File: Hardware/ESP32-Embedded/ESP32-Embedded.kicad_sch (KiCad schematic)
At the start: 20 parts, among them J1 10103592-0001LF, Q1 S8050, Q2 S8050, U1 ESP32-WROOM-32E, U2 AMS1117-3.3, U3 CH340G

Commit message: sch casi terminado ordene y agregue pocas cosas
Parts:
- added R6: 10K, EESTN5:R_1206, symbol Device:R
- added SW1, SW2: SW_Push, symbol EESTN5:SW_Push
- C6: value C_Small -> 100nF
- J1: value 10103592-0001LF -> Micro USB
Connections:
- net +3V3: now also R6.2
- net EN: now also SW1.2
- net GND: now also SW1.1, SW2.1
- net IO0: now also R6.1, SW2.2
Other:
- note added: "Alimentacion"
- note added: "Conversor UART/Serial"
- note added: "ESP32 WROOM 32"
- note added: "Pulsadores EN y BOOT , y Led test Blink"
- moved on the sheet: C1, C2, C3, C4, C5, C6, D1, J1, LED1, LED2, Q1, Q2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

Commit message: sch terminado
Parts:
- added C7, C8: 22pF, symbol Device:C_Small
- added C9: 100nF, symbol Device:C_Small
- added Y1: 12Mhz, symbol Device:Crystal
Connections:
- net +3V3: now also C9.2
- net GND: now also C7.2, C8.2, C9.1
- net at U3.7 (XI): now also C7.1, Y1.1
- net at U3.8 (XO): now also C8.1, Y1.2
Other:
- moved on the sheet: C5

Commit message: agregue foots ,inicie pcb ordene componentes
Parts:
- C1, C3: footprint EESTN5:C_0805 -> Capacitor_THT:CP_Radial_D4.0mm_P1.50mm
- C5, C9: footprint (none) -> EESTN5:C_0805
- C6: renamed from C7; footprint (none) -> EESTN5:C_1206
- C7: renamed from C8; footprint (none) -> EESTN5:C_1206
- C8: renamed from C6; footprint (none) -> EESTN5:C_0805
- D1: footprint (none) -> Diode_SMD:D_SMF
- J1: footprint AMPHENOL_10103592-0001LF -> MICROUSB FOOT:AMPHENOL_10103592-0001LF
- Q1, Q2: footprint Package_TO_SOT_THT:TO-92_Inline -> SS8050:SOT-23_BEC
- R2, R3: footprint (none) -> EESTN5:R_1206
- SW1, SW2: footprint (none) -> Button_Switch_SMD:SW_SPST_B3U-1000P-B
- U1: footprint footprints:ESP32-WROOM-32E -> ESP32-WROOM-32D:MODULE_ESP32-WROOM-32D
- U2: footprint footprints:SOT-223-3_TabPin2 -> Package_TO_SOT_SMD:SOT-223-3_TabPin2
- Y1: footprint (none) -> Crystal:Crystal_SMD_3215-2Pin_3.2x1.5mm
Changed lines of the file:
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@@
   (symbol (lib_id "Device:C_Small") (at 202.565 48.514 0) (unit 1)
     (in_bom yes) (on_board yes) (dnp no) (fields_autoplaced)
-    (property "Reference" "C6" (at 204.8891 47.8766 0)
+    (property "Reference" "C8" (at 204.8891 47.8766 0)
       (effects (font (size 1.27 1.27)) (justify left))
     )
@@
       (effects (font (size 1.27 1.27)) (justify left))
     )
-    (property "Footprint" "" (at 202.565 48.514 0)
+    (property "Footprint" "EESTN5:C_0805" (at 202.565 48.514 0)
       (effects (font (size 1.27 1.27)) hide)
     )
@@
       (project "ESP32-Embedded"
         (path "/44ee4593-0772-40e5-aa53-983b9011845a"
-          (reference "C6") (unit 1)
+          (reference "C8") (unit 1)
         )
       )
@@
       (effects (font (size 1.27 1.27)) (justify left))
     )
-    (property "Footprint" "EESTN5:C_0805" (at 61.6712 120.523 0)
+    (property "Footprint" "Capacitor_THT:CP_Radial_D4.0mm_P1.50mm" (at 61.6712 120.523 0)
       (effects (font (size 1.27 1.27)) hide)
     )
@@
   (symbol (lib_id "Device:C_Small") (at 15.24 63.627 0) (unit 1)
     (in_bom yes) (on_board yes) (dnp no)
-    (property "Reference" "C7" (at 18.796 63.373 0)
+    (property "Reference" "C6" (at 18.796 63.373 0)
       (effects (font (size 1.27 1.27)))
     )
@@
       (effects (font (size 1.27 1.27)))
     )
-    (property "Footprint" "" (at 15.24 63.627 0)
+    (property "Footprint" "EESTN5:C_1206" (at 15.24 63.627 0)
       (effects (font (size 1.27 1.27)) hide)
     )
@@
       (project "ESP32-Embedded"
         (path "/44ee4593-0772-40e5-aa53-983b9011845a"
-          (reference "C7") (unit 1)
+          (reference "C6") (unit 1)
         )
       )
@@
       (effects (font (size 1.27 1.27)))
     )
-    (property "Footprint" "" (at 21.082 57.658 0)
+    (property "Footprint" "Crystal:Crystal_SMD_3215-2Pin_3.2x1.5mm" (at 21.082 57.658 0)
       (effects (font (size 1.27 1.27)) hide)
     )
@@
       (effects (font (size 1.27 1.27)))
     )
-    (property "Footprint" "AMPHENOL_10103592-0001LF" (at 24.257 117.729 0)
+    (property "Footprint" "MICROUSB FOOT:AMPHENOL_10103592-0001LF" (at 24.257 117.729 0)
       (effects (font (size 1.27 1.27)) (justify bottom) hide)
     )
@@
       (effects (font (size 1.27 1.27)))
     )
-    (property "Footprint" "" (at 127.381 44.577 0)
+    (property "Footprint" "EESTN5:C_0805" (at 127.381 44.577 0)
       (effects (font (size 1.27 1.27)) hide)
     )
@@
       (effects (font (size 1.27 1.27)))
     )
-    (property "Footprint" "footprints:SOT-223-3_TabPin2" (at 78.486 106.553 0)
+    (property "Footprint" "Package_TO_SOT_SMD:SOT-223-3_TabPin2" (at 78.486 106.553 0)
       (effects (font (size 1.27 1.27)) hide)
     )
@@
       (effects (font (size 1.27 1.27)) (justify left))
     )
-    (property "Footprint" "Package_TO_SOT_THT:TO-92_Inline" (at 93.345 43.18 0)
+    (property "Footprint" "SS8050:SOT-23_BEC" (at 93.345 43.18 0)
       (effects (font (size 1.27 1.27) italic) (justify left) hide)
     )
@@
       (effects (font (size 1.27 1.27)))
     )
-    (property "Footprint" "" (at 77.089 41.275 0)
+    (property "Footprint" "EESTN5:R_1206" (at 77.089 41.275 0)
       (effects (font (size 1.27 1.27)) hide)
     )
@@
       (effects (font (size 1.27 1.27)))
     )
-    (property "Footprint" "" (at 42.545 125.349 0)
+    (property "Footprint" "Diode_SMD:D_SMF" (at 42.545 125.349 0)
       (effects (font (size 1.27 1.27)) hide)
     )
@@
   (symbol (lib_id "Device:C_Small") (at 25.781 63.881 0) (unit 1)
     (in_bom yes) (on_board yes) (dnp no)
-    (property "Reference" "C8" (at 29.083 65.405 0)
+    (property "Reference" "C7" (at 29.083 65.405 0)
       (effects (font (size 1.27 1.27)))
     )
@@
       (effects (font (size 1.27 1.27)))
     )
-    (property "Footprint" "" (at 25.781 63.881 0)
+    (property "Footprint" "EESTN5:C_1206" (at 25.781 63.881 0)
       (effects (font (size 1.27 1.27)) hide)
     )
@@
       (project "ESP32-Embedded"
         (path "/44ee4593-0772-40e5-aa53-983b9011845a"
-          (reference "C8") (unit 1)
+          (reference "C7") (unit 1)
         )
       )
@@
       (effects (font (size 1.27 1.27)) (justify left))
     )
-    (property "Footprint" "Package_TO_SOT_THT:TO-92_Inline" (at 93.345 60.198 0)
+    (property "Footprint" "SS8050:SOT-23_BEC" (at 93.345 60.198 0)
       (effects (font (size 1.27 1.27) italic) (justify left) hide)
     )
@@
       (effects (font (size 1.27 1.27)))
     )
-    (property "Footprint" "" (at 77.089 58.293 0)
+    (property "Footprint" "EESTN5:R_1206" (at 77.089 58.293 0)
       (effects (font (size 1.27 1.27)) hide)
     )
@@
       (effects (font (size 1.27 1.27)) hide)
     )
-    (property "Footprint" "" (at 235.585 54.737 0)
-      (effects (font (size 1.27 1.27)))
+    (property "Footprint" "Button_Switch_SMD:SW_SPST_B3U-1000P-B" (at 235.585 54.737 0)
+      (effects (font (size 1.27 1.27)) hide)
     )
     (property "Datasheet" "" (at 235.585 54.737 0)
@@
       (effects (font (size 1.27 1.27)) hide)
     )
-    (property "Footprint" "" (at 216.281 54.61 0)
-      (effects (font (size 1.27 1.27)))
+    (property "Footprint" "Button_Switch_SMD:SW_SPST_B3U-1000P-B" (at 216.281 54.61 0)
+      (effects (font (size 1.27 1.27)) hide)
     )
     (property "Datasheet" "" (at 216.281 54.61 0)
@@
   (symbol (lib_id "Device:C_Small") (at 51.435 64.008 270) (unit 1)
     (in_bom yes) (on_board yes) (dnp no)
-    (property "Reference" "C5" (at 49.911 67.818 90)
+    (property "Reference" "C5" (at 48.006 67.818 90)
       (effects (font (size 1.27 1.27)))
     )
@@
       (effects (font (size 1.27 1.27)))
     )
-    (property "Footprint" "" (at 51.435 64.008 0)
+    (property "Footprint" "EESTN5:C_0805" (at 51.435 64.008 0)
       (effects (font (size 1.27 1.27)) hide)
     )
@@
       (effects (font (size 1.27 1.27)) (justify left))
     )
-    (property "Footprint" "EESTN5:C_0805" (at 89.3572 120.523 0)
+    (property "Footprint" "Capacitor_THT:CP_Radial_D4.0mm_P1.50mm" (at 89.3572 120.523 0)
       (effects (font (size 1.27 1.27)) hide)
     )
@@
       (effects (font (size 1.27 1.27)) (justify left))
     )
-    (property "Footprint" "footprints:ESP32-WROOM-32E" (at 152.019 67.183 0)
+    (property "Footprint" "ESP32-WROOM-32D:MODULE_ESP32-WROOM-32D" (at 152.019 67.183 0)
       (effects (font (size 1.27 1.27)) (justify bottom) hide)
     )

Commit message: ordenando componentes en placa
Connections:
- net +3V3: now also U1.2 (3V3); no longer U1.3V3
- net DTR: now also Q1.E; no longer Q1.1 (E)
- net EN: now also Q2.C, U1.3 (EN); no longer Q2.3 (C), U1.9 (EN)
- net GND: now also U1.1 (GND), U1.15 (GND), U1.38 (GND)
- net IO0: now also Q1.C, U1.25 (IO0); no longer Q1.3 (C), U1.23 (IO0)
- net IO2: now also U1.24 (IO2); no longer U1.22 (IO2)
- net RTS: now also Q2.E; no longer Q2.1 (E)
- net RXD0: now also U1.34 (RXD0); no longer U1.40 (RXD0)
- net TXD0: now also U1.35 (TXD0); no longer U1.41 (TXD0)
- net at R2.2: now also Q1.B; no longer Q1.2 (B)
- net at R3.2: now also Q2.B; no longer Q2.2 (B)
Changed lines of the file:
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@@
     (stroke (width 0) (type default))
   )
+  (wire (pts (xy 141.859 95.631) (xy 141.859 93.853))
+    (stroke (width 0) (type default))
+  )
   (wire (pts (xy 39.624 64.008) (xy 39.624 62.738))
     (stroke (width 0) (type default))
@@
     )
   )
-  (symbol (lib_id "Transistor_BJT:S8050") (at 88.265 41.275 0) (unit 1)
+  (symbol (lib_name "S8050_1") (lib_id "Transistor_BJT:S8050") (at 88.265 41.275 0) (unit 1)
     (in_bom yes) (on_board yes) (dnp no) (fields_autoplaced)
     (property "Reference" "Q1" (at 93.1164 40.6313 0)
@@
       (effects (font (size 1.27 1.27)) (justify left) hide)
     )
-    (pin "1")
-    (pin "2")
-    (pin "3")
+    (pin "B")
+    (pin "C")
+    (pin "E")
     (instances
       (project "ESP32-Embedded"
@@
     )
   )
-  (symbol (lib_id "Transistor_BJT:S8050") (at 88.265 58.293 0) (unit 1)
-    (in_bom yes) (on_board yes) (dnp no) (fields_autoplaced)
-    (property "Reference" "Q2" (at 93.1164 57.6493 0)
-      (effects (font (size 1.27 1.27)) (justify left))
-    )
-    (property "Value" "S8050" (at 93.1164 59.5703 0)
-      (effects (font (size 1.27 1.27)) (justify left))
-    )
-    (property "Footprint" "SS8050:SOT-23_BEC" (at 93.345 60.198 0)
-      (effects (font (size 1.27 1.27) italic) (justify left) hide)
-    )
-    (property "Datasheet" "http://www.unisonic.com.tw/datasheet/S8050.pdf" (at 88.265 58.293 0)
-      (effects (font (size 1.27 1.27)) (justify left) hide)
-    )
-    (pin "1")
-    (pin "2")
-    (pin "3")
-    (instances
-      (project "ESP32-Embedded"
-        (path "/44ee4593-0772-40e5-aa53-983b9011845a"
-          (reference "Q2") (unit 1)
-        )
-      )
-    )
-  )
   (symbol (lib_id "Device:R") (at 202.565 39.37 180) (unit 1)
     (in_bom yes) (on_board yes) (dnp no) (fields_autoplaced)
@@
     )
   )
+  (symbol (lib_id "power:GND") (at 141.859 95.631 0) (unit 1)
+    (in_bom yes) (on_board yes) (dnp no)
+    (property "Reference" "#PWR020" (at 141.859 101.981 0)
+      (effects (font (size 1.27 1.27)) hide)
+    )
+    (property "Value" "GND" (at 141.859 99.441 0)
+      (effects (font (size 1.27 1.27)))
+    )
+    (property "Footprint" "" (at 141.859 95.631 0)
+      (effects (font (size 1.27 1.27)) hide)
+    )
+    (property "Datasheet" "" (at 141.859 95.631 0)
+      (effects (font (size 1.27 1.27)) hide)
+    )
+    (pin "1")
+    (instances
+      (project "ESP32-Embedded"
+        (path "/44ee4593-0772-40e5-aa53-983b9011845a"
+          (reference "#PWR020") (unit 1)
+        )
+      )
+      (project "Esp32Modulo"
+        (path "/d8ce7d9a-219e-40d1-b957-d72bdccbdc30"
+          (reference "#PWR010") (unit 1)
+        )
+      )
+    )
+  )
   (symbol (lib_id "power:GND") (at 240.665 61.849 0) (unit 1)
     (in_bom yes) (on_board yes) (dnp no) (fields_autoplaced)
@@
     )
   )
+  (symbol (lib_name "S8050_1") (lib_id "Transistor_BJT:S8050") (at 88.265 58.293 0) (unit 1)
+    (in_bom yes) (on_board yes) (dnp no) (fields_autoplaced)
+    (property "Reference" "Q2" (at 93.1164 57.6493 0)
+      (effects (font (size 1.27 1.27)) (justify left))
+    )
+    (property "Value" "S8050" (at 93.1164 59.5703 0)
+      (effects (font (size 1.27 1.27)) (justify left))
+    )
+    (property "Footprint" "SS8050:SOT-23_BEC" (at 93.345 60.198 0)
+      (effects (font (size 1.27 1.27) italic) (justify left) hide)
+    )
+    (property "Datasheet" "http://www.unisonic.com.tw/datasheet/S8050.pdf" (at 88.265 58.293 0)
+      (effects (font (size 1.27 1.27)) (justify left) hide)
+    )
+    (pin "B")
+    (pin "C")
+    (pin "E")
+    (instances
+      (project "ESP32-Embedded"
+        (path "/44ee4593-0772-40e5-aa53-983b9011845a"
+          (reference "Q2") (unit 1)
+        )
+      )
+    )
+  )
   (symbol (lib_id "power:+3V3") (at 58.928 62.992 0) (unit 1)
     (in_bom yes) (on_board yes) (dnp no)
@@
       (effects (font (size 1.27 1.27)) hide)
     )
+    (pin "6")
+    (pin "7")
+    (pin "8")
+    (pin "9")
     (pin "10")
     (pin "11")
@@
     (pin "13")
     (pin "14")
-    (pin "15")
     (pin "16")
-    (pin "17")
-    (pin "18")
-    (pin "20")
-    (pin "21")
-    (pin "22")
     (pin "23")
     (pin "24")
     (pin "25")
+    (pin "26")
     (pin "27")
     (pin "28")
+    (pin "17")
+    (pin "18")
+    (pin "19")
+    (pin "20")
+    (pin "21")
+    (pin "22")
     (pin "29")
     (pin "30")
+    (pin "37")
     (pin "31")
-    (pin "32")
-    (pin "33")
+    (pin "36")
+    (pin "2")
     (pin "34")
     (pin "35")
-    (pin "36")
-    (pin "38")
-    (pin "39")
-    (pin "3V3")
-    (pin "40")
-    (pin "41")
-    (pin "42")
+    (pin "33")
+    (pin "4")
     (pin "5")
-    (pin "8")
-    (pin "9")
-    (pin "GND")
-    (pin "GND")
-    (pin "GND")
+    (pin "3")
+    (pin "1")
+    (pin "15")
     (pin "GND")
     (pin "GND")
@@
     (pin "GND")
     (pin "GND")
-    (pin "NC")
+    (pin "38")
+    (pin "32")
     (instances
       (project "ESP32-Embedded"

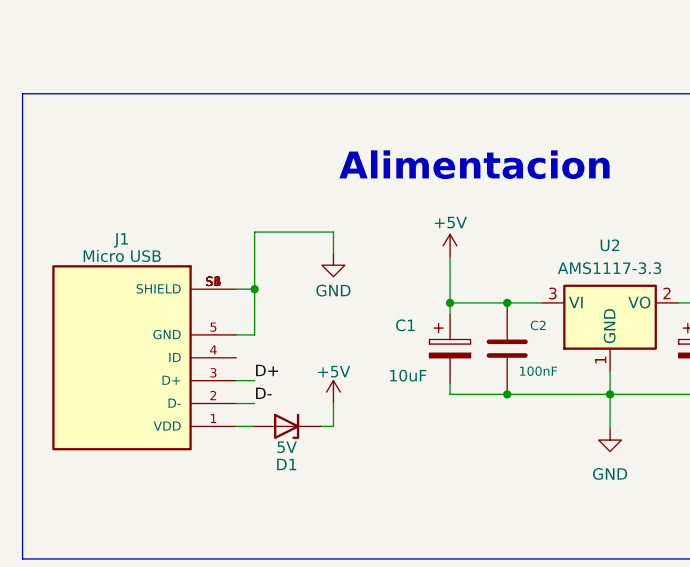
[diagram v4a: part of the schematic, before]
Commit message: placa con esp32 embebido y 5 puentes lista
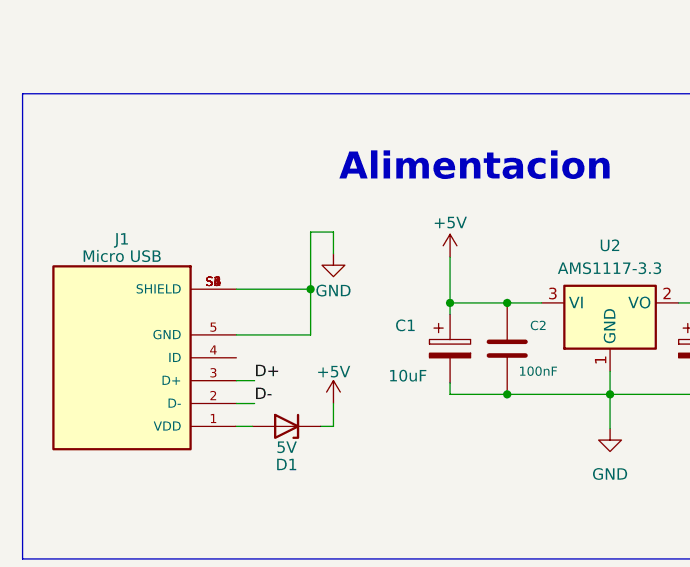
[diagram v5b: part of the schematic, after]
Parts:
- C2, C4, C5, C8, C9: footprint EESTN5:C_0805 -> EESTN5:C_1206
- R2, R3: footprint EESTN5:R_1206 -> EESTN5:RES0.2
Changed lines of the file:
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@@
   (junction (at 67.056 121.793) (diameter 0) (color 0 0 0 0)
   )
+  (junction (at 45.212 110.109) (diameter 0) (color 0 0 0 0)
+  )
   (junction (at 25.781 57.658) (diameter 0) (color 0 0 0 0)
   )
@@
   (junction (at 39.624 64.008) (diameter 0) (color 0 0 0 0)
   )
-  (junction (at 38.989 110.109) (diameter 0) (color 0 0 0 0)
-  )
   (junction (at 15.24 57.658) (diameter 0) (color 0 0 0 0)
   )
@@
     (stroke (width 0) (type default))
   )
-  (wire (pts (xy 36.957 115.189) (xy 38.989 115.189))
+  (wire (pts (xy 36.957 115.189) (xy 45.212 115.189))
     (stroke (width 0) (type default))
   )
@@
     (stroke (width 0) (type default))
   )
+  (wire (pts (xy 45.212 110.109) (xy 45.212 115.189))
+    (stroke (width 0) (type default))
+  )
   (wire (pts (xy 39.624 30.861) (xy 39.624 32.258))
     (stroke (width 0) (type default))
@@
     (stroke (width 0) (type default))
   )
-  (wire (pts (xy 38.989 110.109) (xy 36.957 110.109))
-    (stroke (width 0) (type default))
-  )
   (wire (pts (xy 69.85 41.275) (xy 74.549 41.275))
     (stroke (width 0) (type default))
@@
     (stroke (width 0) (type default))
   )
-  (wire (pts (xy 38.989 103.759) (xy 47.752 103.759))
+  (wire (pts (xy 45.212 103.759) (xy 47.752 103.759))
     (stroke (width 0) (type default))
   )
@@
     (stroke (width 0) (type default))
   )
-  (wire (pts (xy 38.989 110.109) (xy 38.989 103.759))
-    (stroke (width 0) (type default))
-  )
   (wire (pts (xy 246.761 44.704) (xy 240.665 44.704))
     (stroke (width 0) (type default))
@@
     (stroke (width 0) (type default))
   )
-  (wire (pts (xy 38.989 115.189) (xy 38.989 110.109))
+  (wire (pts (xy 45.212 103.759) (xy 45.212 110.109))
+    (stroke (width 0) (type default))
+  )
+  (wire (pts (xy 36.957 110.109) (xy 45.212 110.109))
     (stroke (width 0) (type default))
   )
@@
       (effects (font (size 1.27 1.27)) (justify left))
     )
-    (property "Footprint" "EESTN5:C_0805" (at 202.565 48.514 0)
+    (property "Footprint" "EESTN5:C_1206" (at 202.565 48.514 0)
       (effects (font (size 1.27 1.27)) hide)
     )
@@
       (effects (font (size 1.27 1.27)))
     )
-    (property "Footprint" "EESTN5:C_0805" (at 127.381 44.577 0)
+    (property "Footprint" "EESTN5:C_1206" (at 127.381 44.577 0)
       (effects (font (size 1.27 1.27)) hide)
     )
@@
       (effects (font (size 1.27 1.27)))
     )
-    (property "Footprint" "EESTN5:R_1206" (at 77.089 41.275 0)
+    (property "Footprint" "EESTN5:RES0.2" (at 77.089 41.275 0)
       (effects (font (size 1.27 1.27)) hide)
     )
@@
       (effects (font (size 1.27 1.27)))
     )
-    (property "Footprint" "EESTN5:R_1206" (at 77.089 58.293 0)
+    (property "Footprint" "EESTN5:RES0.2" (at 77.089 58.293 0)
       (effects (font (size 1.27 1.27)) hide)
     )
@@
       (effects (font (size 1.016 1.016)) (justify left))
     )
-    (property "Footprint" "EESTN5:C_0805" (at 97.2312 120.523 0)
+    (property "Footprint" "EESTN5:C_1206" (at 97.2312 120.523 0)
       (effects (font (size 0.762 0.762)) hide)
     )
@@
       (effects (font (size 1.27 1.27)))
     )
-    (property "Footprint" "EESTN5:C_0805" (at 51.435 64.008 0)
+    (property "Footprint" "EESTN5:C_1206" (at 51.435 64.008 0)
       (effects (font (size 1.27 1.27)) hide)
     )
@@
       (effects (font (size 1.016 1.016)) (justify left))
     )
-    (property "Footprint" "EESTN5:C_0805" (at 68.0212 120.523 0)
+    (property "Footprint" "EESTN5:C_1206" (at 68.0212 120.523 0)
       (effects (font (size 0.762 0.762)) hide)
     )
@@
       (effects (font (size 1.27 1.27)) hide)
     )
-    (pin "6")
-    (pin "7")
-    (pin "8")
-    (pin "9")
+    (pin "1")
     (pin "10")
     (pin "11")
@@
     (pin "13")
     (pin "14")
+    (pin "15")
     (pin "16")
-    (pin "23")
-    (pin "24")
-    (pin "25")
-    (pin "26")
-    (pin "27")
-    (pin "28")
     (pin "17")
     (pin "18")
     (pin "19")
+    (pin "2")
     (pin "20")
     (pin "21")
     (pin "22")
+    (pin "23")
+    (pin "24")
+    (pin "25")
+    (pin "26")
+    (pin "27")
+    (pin "28")
     (pin "29")
+    (pin "3")
     (pin "30")
-    (pin "37")
     (pin "31")
-    (pin "36")
-    (pin "2")
+    (pin "32")
+    (pin "33")
     (pin "34")
     (pin "35")
-    (pin "33")
+    (pin "36")
+    (pin "37")
+    (pin "38")
     (pin "4")
     (pin "5")
-    (pin "3")
-    (pin "1")
-    (pin "15")
+    (pin "6")
+    (pin "7")
+    (pin "8")
+    (pin "9")
     (pin "GND")
     (pin "GND")
@@
     (pin "GND")
     (pin "GND")
-    (pin "38")
-    (pin "32")
     (instances
       (project "ESP32-Embedded"
